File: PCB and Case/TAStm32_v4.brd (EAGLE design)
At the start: 50 x 100 mm, 53 parts, among them IC1 74LVCH2T45DC,125, IC2 74LVCH2T45DC,125, IC3 74LVCH2T45DC,125, IC4 74LVCH2T45DC,125, IC5 74LVCH2T45DC,125, IC6 74LVCH2T45DC,125, J1 ZX62D-B-5PA8, J10 RJSSE538002, J11 RJSSE538002, J12 SOICBITE, J13 CONSOLE_RESET, J2 UE27-AC54-100, J4 CONSOLE_RESET, J5 95278-802A12LF, J6 SAMTEC-TSM-116-01-X-SVJ, J7 SAMTEC-TSM-116-01-X-SVJ, U1 STM32F446RET6, U2 3.3V REG, Y1 8MHz

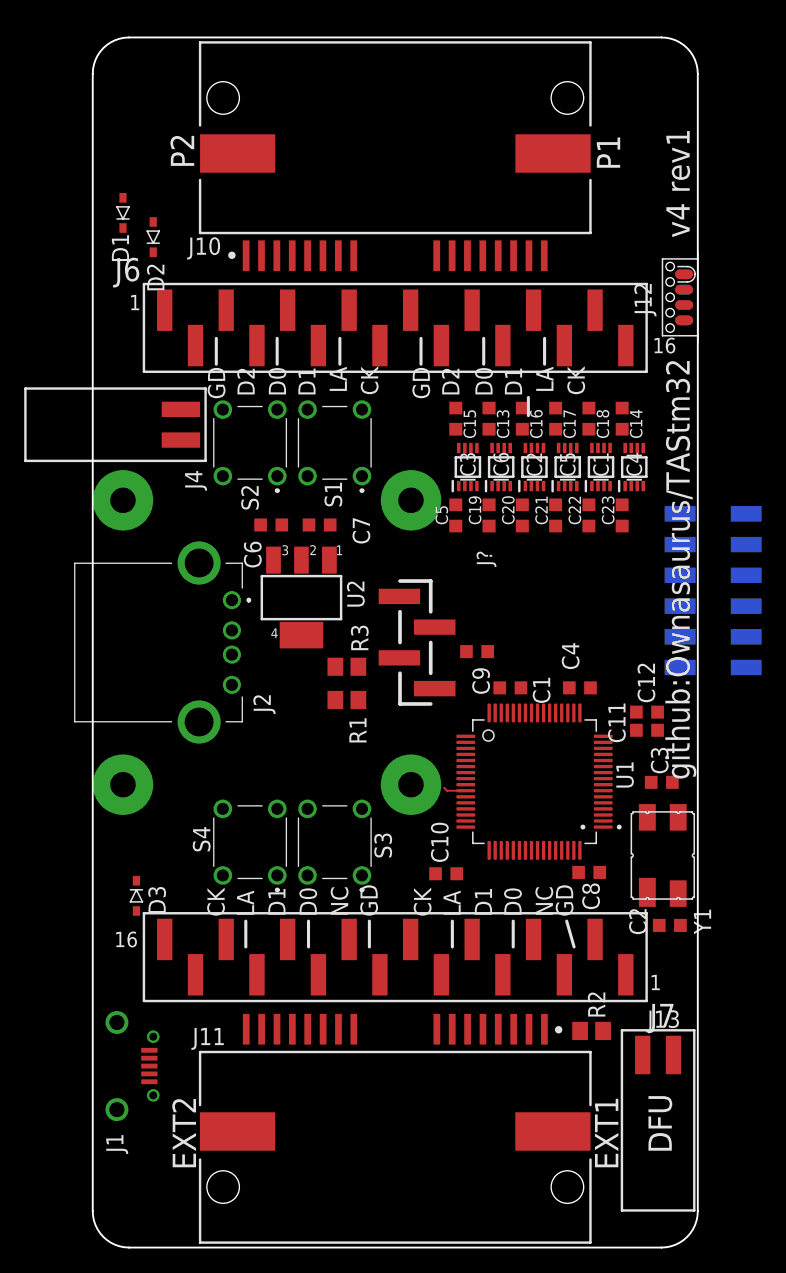
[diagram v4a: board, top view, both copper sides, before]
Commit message: another different level converter, routing
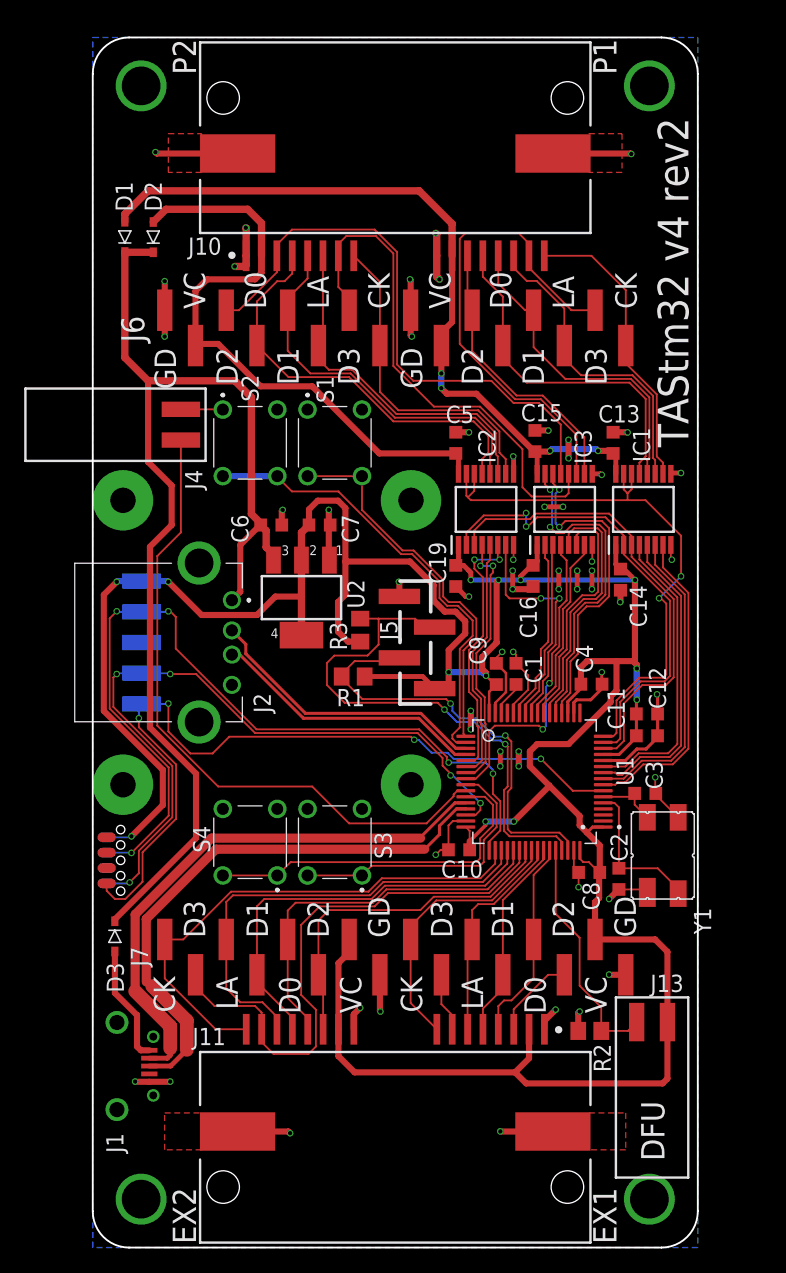
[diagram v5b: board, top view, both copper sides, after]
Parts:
- removed C17, C18, C20, C21, C22, C23: 100nF, rcl:C0603K
- removed IC4, IC5, IC6: 74LVCH2T45DC,125, SamacSys_Parts:SOP50P310X100-8N
- removed J?: OLED128X64, TAStm32_v4:OLED
- added J3: TSM-105-02-L-SHJ, TSM-105-02-L-SH:TSM-105-02-L-SH
- IC1, IC2, IC3: value 74LVCH2T45DC,125 -> 74AVCH4T245PW,118; device SamacSys_Parts:SOP50P310X100-8N -> SamacSys_Parts:SOP65P640X110-16N
- J5: value 95278-802A12LF -> OLED128X64; device SamacSys_Parts:95278802A12LF -> TAStm32_v4:OLED
- moved J12 67.7 mm to (0.40, 32.0), flipped to the bottom
- moved J5 35.0 mm to (16.5, 50.0), flipped to the top
- moved C14 13.3 mm to (43.6, 55.2), turned to 90 degrees
- moved C16 13.0 mm to (36.4, 55.5), turned to 90 degrees
- moved C13 10.4 mm to (43.0, 66.5)
- moved IC3 8.73 mm to (39.0, 61.0)
- moved C15 6.80 mm to (36.5, 66.7)
- moved C5 6.00 mm to (30.0, 66.5), turned to 270 degrees
- moved C19 5.71 mm to (30.0, 55.5)
- moved C2 5.70 mm to (43.5, 30.5), turned to 90 degrees
- moved IC2 5.32 mm to (32.5, 61.0)
- moved IC1 4.95 mm to (45.5, 61.0)
- moved D3 3.79 mm to (1.83, 25.7)
- moved R3 3.22 mm to (22.1, 51.0), turned to 270 degrees
- moved J13 2.76 mm to (46.2, 13.3)
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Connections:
- net V1_NC renamed V1_D3
- net V1_NC2 renamed V1_D2
- removed net N$2: S4.1, S4.2, U1.2
- removed net N$3: S3.1, S3.2, U1.3
- removed net N$4: S2.3, S2.4, U1.22
- removed net N$6: S1.3, S1.4, U1.23
- removed net N$8: IC5.3
- removed net N$9: IC6.3
- removed net PA0: J5.11, U1.14
- removed net PA1: J5.12, U1.15
- removed net PA10: U1.43
- removed net PA2: J5.10, U1.16
- removed net PA3: J5.8, U1.17
- removed net PA4: J5.6, U1.20
- removed net PA5: J5.4, U1.21
- removed net PA8: J5.2, U1.41
- removed net V2_NC: J11.15, J7.15
- removed net V2_NC2: J11.11, J7.11
- new net DIR_CLKLAT: IC1.3, IC2.3, U1.14
- new net ENABLE_D0D1: IC1.14, IC1.15, IC2.14, IC2.15, U1.16
- new net ENABLE_P1D2D3: IC3.15, U1.21
- new net ENABLE_P2D2D3: IC3.14, U1.20
- new net SWITCH1: S1.3, S1.4, U1.33
- new net SWITCH2: S2.3, S2.4, U1.34
- new net SWITCH3: S3.1, S3.2, U1.41
- new net SWITCH4: S4.1, S4.2, U1.43
- new net V2_D2: J11.11, J7.11, U1.55
- new net V2_D3: J11.15, J7.15, U1.54
- net DIR_D0D1: now also IC1.2, IC2.2, U1.15; no longer IC1.5, IC3.5
- net DIR_P1D2D3: now also IC3.2, U1.27; no longer IC5.5
- net DIR_P2D2D3: now also IC3.3, U1.26; no longer IC6.5
- net GND: now also IC1.8, IC1.9, IC2.8, IC2.9, IC3.8, IC3.9, J3.3, J5.1, J5.6, J5.7, J5.8; no longer C17.1, C18.1, C20.1, C21.1, C22.1, C23.1, IC1.4, IC2.4, IC3.4, IC4.4, IC5.4, IC6.4, J?.1, J?.5, J?.6, J?.7, J?.8
- net I2C_SCL: now also J5.2; no longer J?.2
- net I2C_SDA: now also J5.3; no longer J?.3
- net NRST: now also J3.5; no longer J5.9
- net P1_5V: now also IC1.16, IC3.16; no longer C14.2, C16.2, C17.2, IC1.8, IC2.8, IC3.8, IC4.8, IC5.8
- net P1_CLOCK: now also IC1.10; no longer IC4.6
- net P1_CLOCK_3V: now also IC1.7; no longer IC4.3
- net P1_D0: now also IC1.13; no longer IC1.7
- net P1_D0_3V: now also IC1.4; no longer IC1.2
- net P1_D1: now also IC1.12; no longer IC1.6
- net P1_D1_3V: now also IC1.5; no longer IC1.3
- net P1_D2: now also IC3.10; no longer IC5.7
- net P1_D2_3V: now also IC3.7
- net P1_D3: now also IC3.11; no longer IC5.6
- net P1_D3_3V: now also IC3.6, U1.23; no longer IC5.2
- net P1_LATCH: now also IC1.11; no longer IC4.7
- net P1_LATCH_3V: now also IC1.6; no longer IC4.2
- net P2_5V: now also C5.2, IC2.16; no longer C18.2, IC6.8
- net P2_CLOCK: now also IC2.10; no longer IC2.6
- net P2_CLOCK_3V: now also IC2.7; no longer IC2.3
- net P2_D0: now also IC2.13; no longer IC3.7
- net P2_D0_3V: now also IC2.4; no longer IC3.2
- net P2_D1: now also IC2.12; no longer IC3.6
- net P2_D1_3V: now also IC2.5; no longer IC3.3
- net P2_D2: now also IC3.13; no longer IC6.7
- net P2_D2_3V: now also IC3.4
- net P2_D3: now also IC3.12; no longer IC6.6
- net P2_D3_3V: now also IC3.5, U1.22; no longer IC6.2
- net P2_LATCH: now also IC2.11; no longer IC2.7
- net P2_LATCH_3V: now also IC2.6; no longer IC2.2
- net SWCLK: now also J3.2; no longer J5.3
- net SWDIO: now also J3.4; no longer J5.7
- net V+: now also C14.2, C16.2, J3.1, J5.4; no longer C20.2, C21.2, C22.2, C23.2, C5.2, IC2.5, IC4.1, IC4.5, IC5.1, IC6.1, J5.1, J?.4
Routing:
- net V+: track 0.00 -> 267.3 mm, vias 0 -> 13
- net GND: track 0.00 -> 132.1 mm, vias 0 -> 63
- net +5V: track 0.00 -> 94.9 mm
- net SWCLK: track 0.00 -> 71.1 mm, vias 0 -> 5
- net NRST: track 0.00 -> 65.3 mm, vias 0 -> 4
- net P1_5V: track 0.00 -> 63.9 mm, vias 0 -> 4
- net SWDIO: track 0.00 -> 59.7 mm, vias 0 -> 5
- net SNES_RESET: track 1.90 -> 54.5 mm
- net P2_5V: track 0.00 -> 51.7 mm
- net ENABLE_D0D1: track 0.00 -> 48.6 mm, vias 0 -> 2
- net P2_D2: track 0.00 -> 47.9 mm
- net V2_D3: track 0.00 -> 46.7 mm
- net DP: track 0.00 -> 46.6 mm
- net DM: track 0.00 -> 45.9 mm
- net I2C_SCL: track 0.00 -> 45.3 mm, vias 0 -> 2
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- added copper zone on layer 1, net GND
- added copper zone on layer 16, net GND
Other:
- board text added: "D3"
- board text added: "EX1"
- board text added: "EX2"
- board text added: "TAStm32 v4 rev2"
- board text added: "VC"
- board text removed: "EXT1"
- board text removed: "EXT2"
- board text removed: "NC"
- board text removed: "github:Ownasaurus/TAStm32"
- board text removed: "v4 rev1"

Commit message: data line series resistors, separate enables for clk/lat, updated ioc file
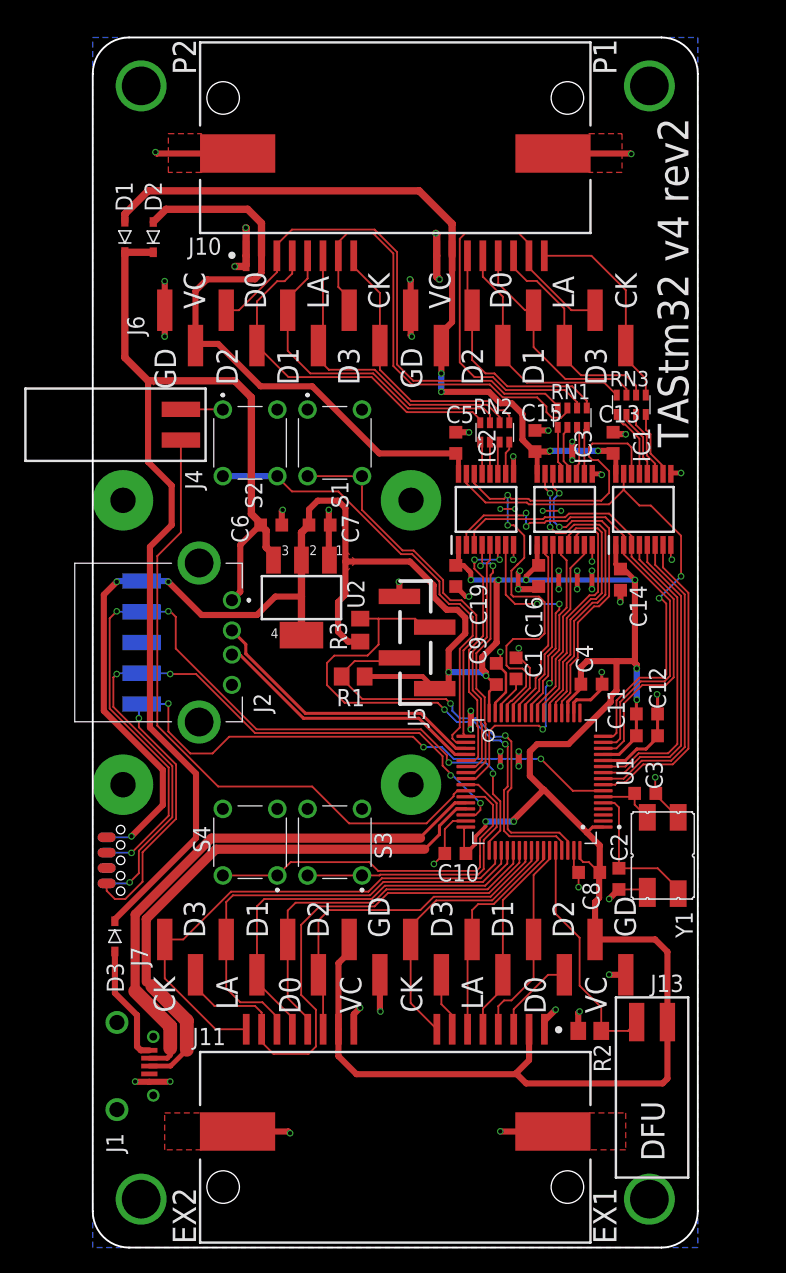
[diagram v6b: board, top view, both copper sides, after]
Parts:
- added RN1, RN2, RN3: CTS742C083, resistor-net:CTS742C083
- moved C1 0.46 mm to (35.0, 47.9)
- moved C16 0.46 mm to (36.8, 55.5)
- moved C10 0.43 mm to (30.0, 32.6)
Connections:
- new net ENABLE_CLKLAT: IC1.14, IC2.14, U1.29
- new net N$10: IC2.10, RN2.4
- new net N$11: IC2.13, RN2.1
- new net N$12: IC1.12, RN3.2
- new net N$13: IC1.11, RN3.3
- new net N$14: IC1.10, RN3.4
- new net N$15: IC1.13, RN3.1
- new net N$2: IC3.13, RN1.1
- new net N$3: IC3.12, RN1.2
- new net N$4: IC3.11, RN1.3
- new net N$6: IC3.10, RN1.4
- new net N$8: IC2.12, RN2.2
- new net N$9: IC2.11, RN2.3
- net ENABLE_D0D1: no longer IC1.14, IC2.14
- net P1_CLOCK: now also RN3.5; no longer IC1.10
- net P1_D0: now also RN3.8; no longer IC1.13
- net P1_D1: now also RN3.7; no longer IC1.12
- net P1_D2: now also RN1.5; no longer IC3.10
- net P1_D3: now also RN1.6; no longer IC3.11
- net P1_LATCH: now also RN3.6; no longer IC1.11
- net P2_CLOCK: now also RN2.5; no longer IC2.10
- net P2_D0: now also RN2.8; no longer IC2.13
- net P2_D1: now also RN2.7; no longer IC2.12
- net P2_D2: now also RN1.8; no longer IC3.13
- net P2_D3: now also RN1.7; no longer IC3.12
- net P2_LATCH: now also RN2.6; no longer IC2.11
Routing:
- net ENABLE_CLKLAT: track 0.00 -> 50.0 mm, vias 0 -> 2
- net P1_D0: track 28.8 -> 19.8 mm
- net P1_D1: track 26.9 -> 18.8 mm
- net P1_LATCH: track 25.8 -> 18.4 mm
- net P1_CLOCK: track 24.4 -> 17.6 mm
- net N$15: track 0.00 -> 5.77 mm
- net N$12: track 0.00 -> 5.62 mm
- net N$13: track 0.00 -> 5.57 mm
- net N$14: track 0.00 -> 5.50 mm
- net P2_D3: track 43.1 -> 37.8 mm
- net P2_D2: track 47.9 -> 43.1 mm
- net ENABLE_D0D1: track 48.6 -> 44.1 mm
- net P2_D0: track 34.5 -> 30.2 mm
- net N$3: track 0.00 -> 4.29 mm
- net N$4: track 0.00 -> 4.05 mm
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- added copper zone on layer 1, net +5V
- added copper zone on layer 1, net V+
